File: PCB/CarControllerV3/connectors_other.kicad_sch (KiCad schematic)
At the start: 38 parts, among them J11 USB_C_Receptacle, J9 USB_C_Receptacle, U14 USBLC6-2P6, U19 USBLC6-2P6, U22 CP2102N-A01-GQFN20R

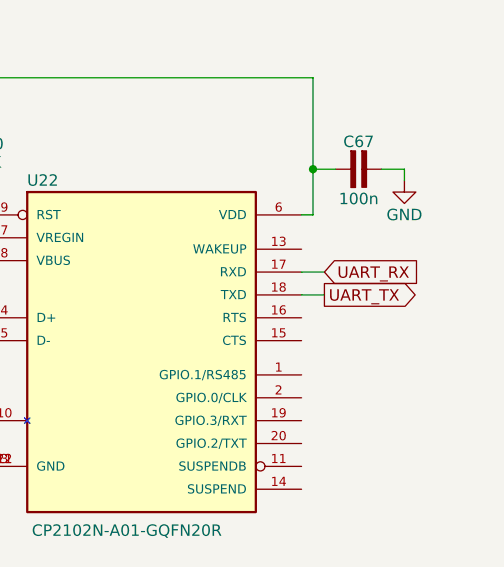
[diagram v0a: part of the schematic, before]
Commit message: More work to PCB
- Rerouted bunch of connections
- Added alternative charge pump circuit
- Bunch of work on analog circuit
- Removed all the capacitor filter on the connectors in favor of filtering when nessesary.
- Placed canbus on JP5.2, JP5.3
- Disconnected various connections that needs to be decided if we should use.
- Added protection to various areas
- Added various todo notes everywhere..
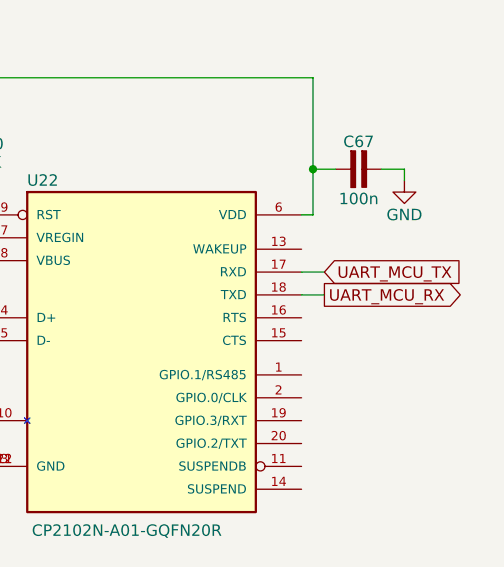
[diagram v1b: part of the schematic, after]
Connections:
- net UART_RX renamed UART_MCU_TX
- net UART_TX renamed UART_MCU_RX
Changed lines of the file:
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@@
 		)
 	)
-	(global_label "UART_RX"
+	(global_label "UART_MCU_TX"
 		(shape input)
 		(at 250.19 58.42 0)
@@
 		)
 		(property "Intersheetrefs" "${INTERSHEET_REFS}"
-			(at 261.279 58.42 0)
+			(at 265.9961 58.42 0)
 			(hide yes)
 			(show_name no)
@@
 		)
 	)
-	(global_label "UART_TX"
+	(global_label "UART_MCU_RX"
 		(shape output)
 		(at 250.19 60.96 0)
@@
 		)
 		(property "Intersheetrefs" "${INTERSHEET_REFS}"
-			(at 260.9766 60.96 0)
+			(at 266.2985 60.96 0)
 			(hide yes)
 			(show_name no)
